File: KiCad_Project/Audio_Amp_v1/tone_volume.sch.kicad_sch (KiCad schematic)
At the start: 29 parts, among them U3 OPA1678

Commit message: Started routing
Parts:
- removed C58, C63: 10u, symbol Device:C_Polarized_US
- removed C60, C61: 100n, symbol Device:C
- removed R15, R18: 100k, symbol Device:R
- removed R22, R23, R24, R25, R27, R29: 10k, symbol Device:R
- removed R26, R28: 3k3, symbol Device:R
- added C48, C49: 10u, Capacitor_SMD:CP_Elec_4x5.8, symbol Device:C_Polarized_US
- added C63, C64: 2n2, Capacitor_SMD:C_0603_1608Metric, symbol Device:C
- added R13, R22, R23, R24, R26, R27: 10k, Resistor_SMD:R_0603_1608Metric, symbol Device:R_US
- added R25, R28: 3k3, Resistor_SMD:R_0603_1608Metric, symbol Device:R_US
- added R29, R33: 100k, Resistor_SMD:R_0603_1608Metric, symbol Device:R_US
- C42, C51: footprint (none) -> Capacitor_SMD:C_0805_2012Metric
- C50, C59, C62: footprint (none) -> Capacitor_SMD:C_0603_1608Metric
- C52, C53: footprint (none) -> Capacitor_SMD:C_1206_3216Metric
- C54, C55: value 2n2 -> 100n; footprint (none) -> Capacitor_SMD:C_1206_3216Metric
- C56, C57: footprint (none) -> Capacitor_SMD:CP_Elec_4x5.8; LCSC (none) -> C116211
- RV1, RV2: footprint (none) -> Potentiometer_THT:Potentiometer_Alps_RK09L_Double_Horizontal; PARTNO (none) -> RK09L1220A1
- RV3: footprint (none) -> Potentiometer_THT:Potentiometer_Alps_RK097_Dual_Horizontal; PARTNO (none) -> RKRK09712200HA
- U3: value OPA1678 -> OPA1678IDR; footprint (none) -> Package_SO:SOIC-8_3.9x4.9mm_P1.27mm
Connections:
- net +12V: now also R29.2
- net DAC_L: now also C48.2; no longer C57.2
- net DAC_R: now also C49.2
- net GNDA: now also R33.1
- net VREF: now also R29.1, R33.2
- net at RV1.5: now also C54.1, C55.1, R27.2
- net at RV1.6: now also C54.2, R24.2
- net at C56.1, U3.1: now also C64.1, R22.2; no longer C54.1
- net at U3.2 (-): now also R23.1, R25.2
- net at RV1.4: now also C55.2, R26.1
- net at C53.2, RV1.1: now also R22.1
- net at C52.1, C53.1, RV1.2: now also R23.2
- net at C52.2, RV1.3: now also R13.2
- net at C62.1, U3.7: now also C57.1, R26.2
- net at C59.2: now also C49.1, R24.1
- net at RV2.5: now also R28.1
- net at U3.6 (-): now also R27.1, R28.2
- net at RV2.3: now also C63.1; no longer C55.1
- net at RV2.2: now also R25.1
- net at RV2.1: now also C64.2; no longer C54.2
- net at RV3.6: now also C57.2
- new net: C48.1, C63.2, R13.1

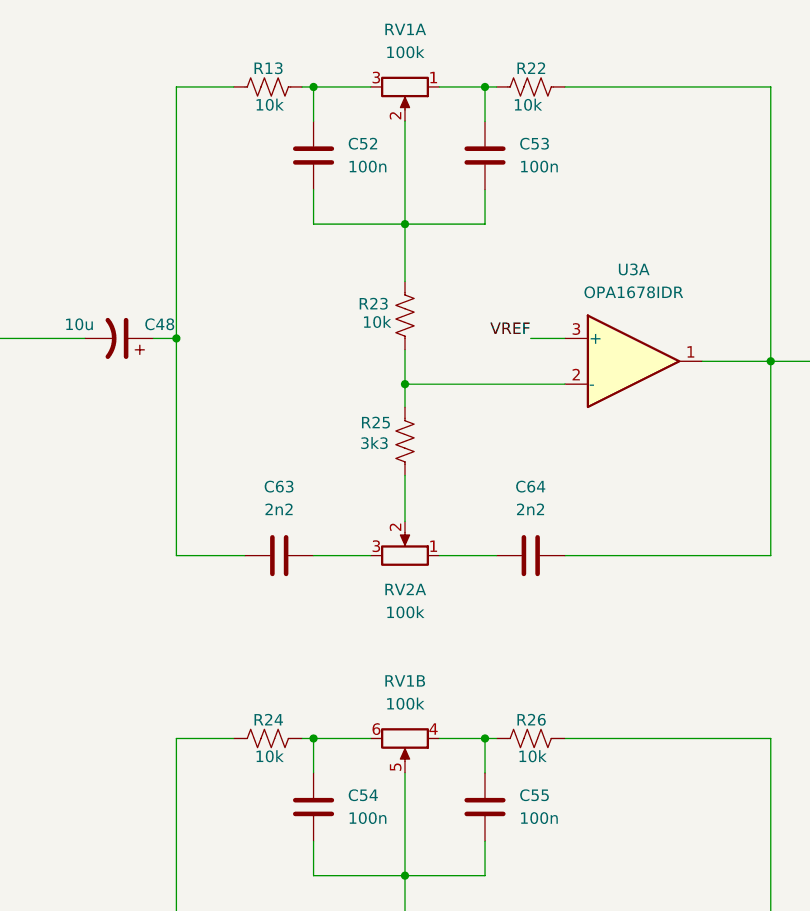
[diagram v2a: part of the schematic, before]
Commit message: added reverse polarity protection
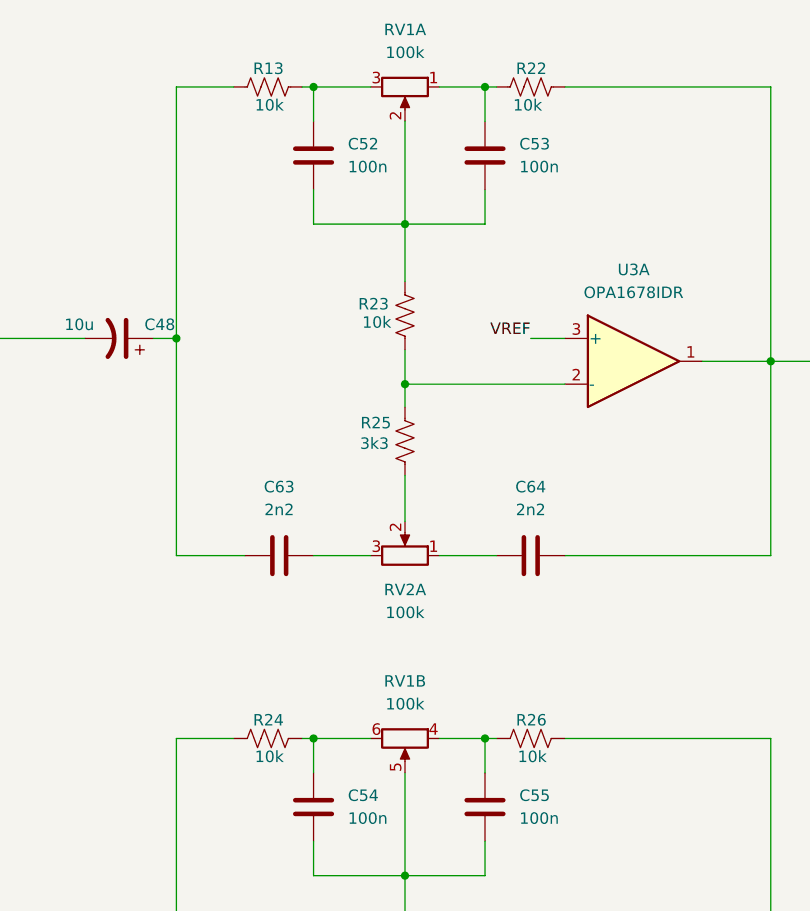
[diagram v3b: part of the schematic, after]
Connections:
- net GNDA: now also RV1.MP (GNDA), RV2.MP (GNDA)
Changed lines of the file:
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@@
 	)
 	(symbol
+		(lib_name "R_Potentiometer_Dual_Separate_1")
 		(lib_id "Device:R_Potentiometer_Dual_Separate")
 		(at 143.51 30.48 270)
@@
 		)
 		(property "Footprint" "Potentiometer_THT:Potentiometer_Alps_RK09L_Double_Horizontal"
-			(at 143.51 30.48 0)
+			(at 142.24 30.48 0)
 			(hide yes)
 			(show_name no)
@@
 		)
 		(pin "6"
+		)
+		(pin "MP"
 		)
 		(instances
@@
 	)
 	(symbol
+		(lib_name "R_Potentiometer_Dual_Separate_2")
 		(lib_id "Device:R_Potentiometer_Dual_Separate")
 		(at 143.51 102.87 270)
@@
 		(in_pos_files yes)
 		(dnp no)
-		(fields_autoplaced yes)
 		(property "Reference" "RV1"
 			(at 143.51 96.52 90)
@@
 		)
 		(property "Footprint" "Potentiometer_THT:Potentiometer_Alps_RK09L_Double_Horizontal"
-			(at 143.51 102.87 0)
+			(at 142.24 102.87 0)
 			(hide yes)
 			(show_name no)
@@
 		)
 		(pin "6"
+		)
+		(pin "MP"
 		)
 		(instances
@@
 	)
 	(symbol
+		(lib_name "R_Potentiometer_Dual_Separate_4")
 		(lib_id "Device:R_Potentiometer_Dual_Separate")
 		(at 143.51 154.94 270)
@@
 		(pin "5"
 		)
+		(pin "MP"
+		)
 		(instances
 			(project "Audio_Amp_v1"
@@
 	)
 	(symbol
+		(lib_name "R_Potentiometer_Dual_Separate_3")
 		(lib_id "Device:R_Potentiometer_Dual_Separate")
 		(at 143.51 82.55 270)
@@
 		(pin "5"
 		)
-		(instances
+		(pin "MP"
+		)
+		(instances

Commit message: Added led into pcb and lyout completed
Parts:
- C42, C51: LCSC (none) -> C84416
- C48, C49, C56, C57: LCSC C116211 -> C445472
- C50: LCSC (none) -> C1591
- C52, C53, C54, C55: LCSC (none) -> C363929
- C59, C62, C63, C64: LCSC (none) -> C33353
- R13, R22, R23, R24, R26, R27: LCSC C25586 -> C98220
- R25, R28: LCSC C25586 -> C2907023
- R29, R33: LCSC C25586 -> C14675
- RV1, RV2: LCSC (none) -> C470470
- RV3: LCSC (none) -> C470545; PARTNO RKRK09712200HA -> RK09712200HA
- U3: LCSC (none) -> C192421
